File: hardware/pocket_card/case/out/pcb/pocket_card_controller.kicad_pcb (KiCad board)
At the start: 2 copper layers, 75 x 37 mm, 17 parts, among them U1 SOIC-28W_7.5x17.9mm_P1.27mm

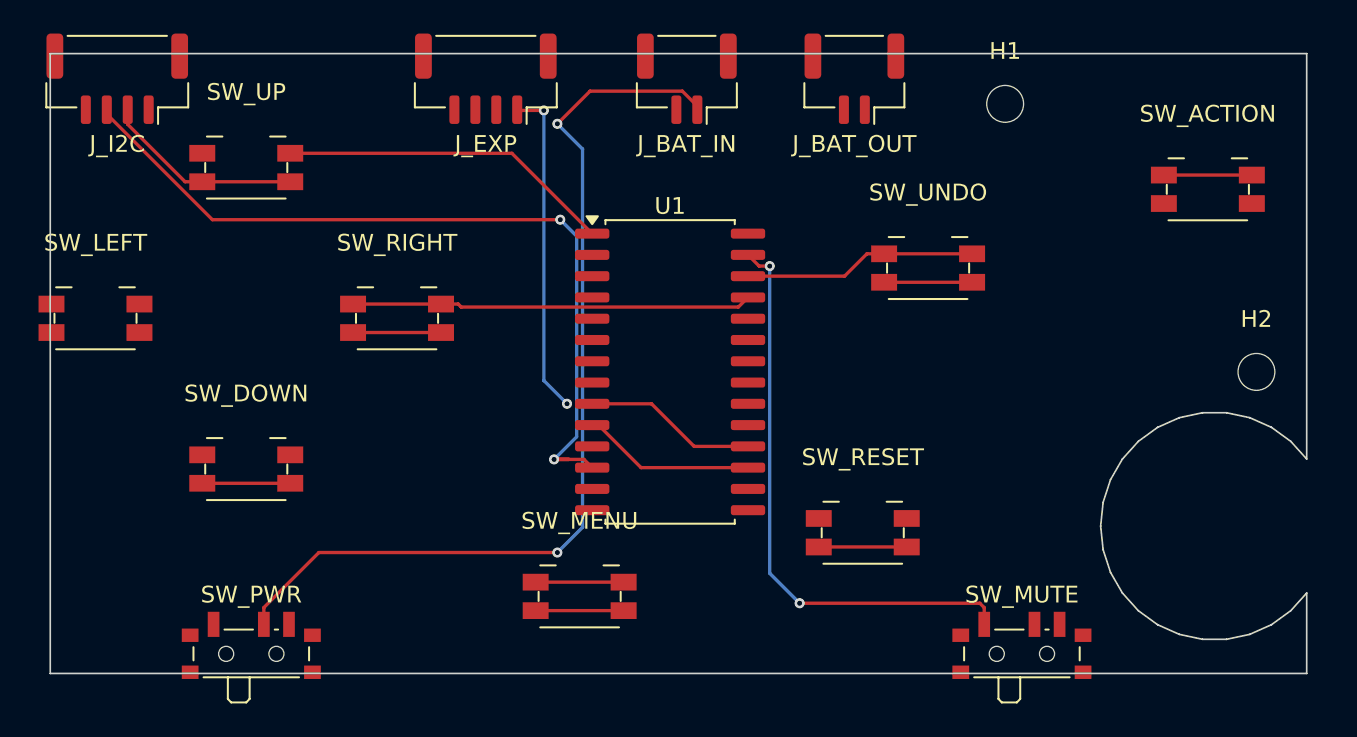
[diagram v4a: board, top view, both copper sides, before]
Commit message: Real grille: the PuzzleScript man; speaker is rectangular
The speaker is 14 x 20 x 3.5 mm, not the disc the geometry had assumed
since the design session. Driver pocket, back-shell fence and PCB notch
are all rectangular now.

That forced the grille to move. At the old (77.5, 81.2) a 14 x 20 driver
overlapped the corner boss by 0.6 mm; at (76, 80) the tightest neighbour
is the Undo collar at +0.6 mm.

The grille is the PuzzleScript man drawn as horizontal slats, generated
from a bitmap in params so the figure can be edited as text:

    01110      head
    01110
    11111      arms
    01110      body
    01010      legs

Runs of 1 are cut and the gaps between rows are the webs holding the
face together. The bottom row is two separate runs, so the five-row
figure is six slots. Square 2.6 mm pixels, 13 x 13 mm overall, sitting
inside the 14 x 20 driver footprint.

Co-Authored-By: Claude Opus 5 <noreply@anthropic.com>
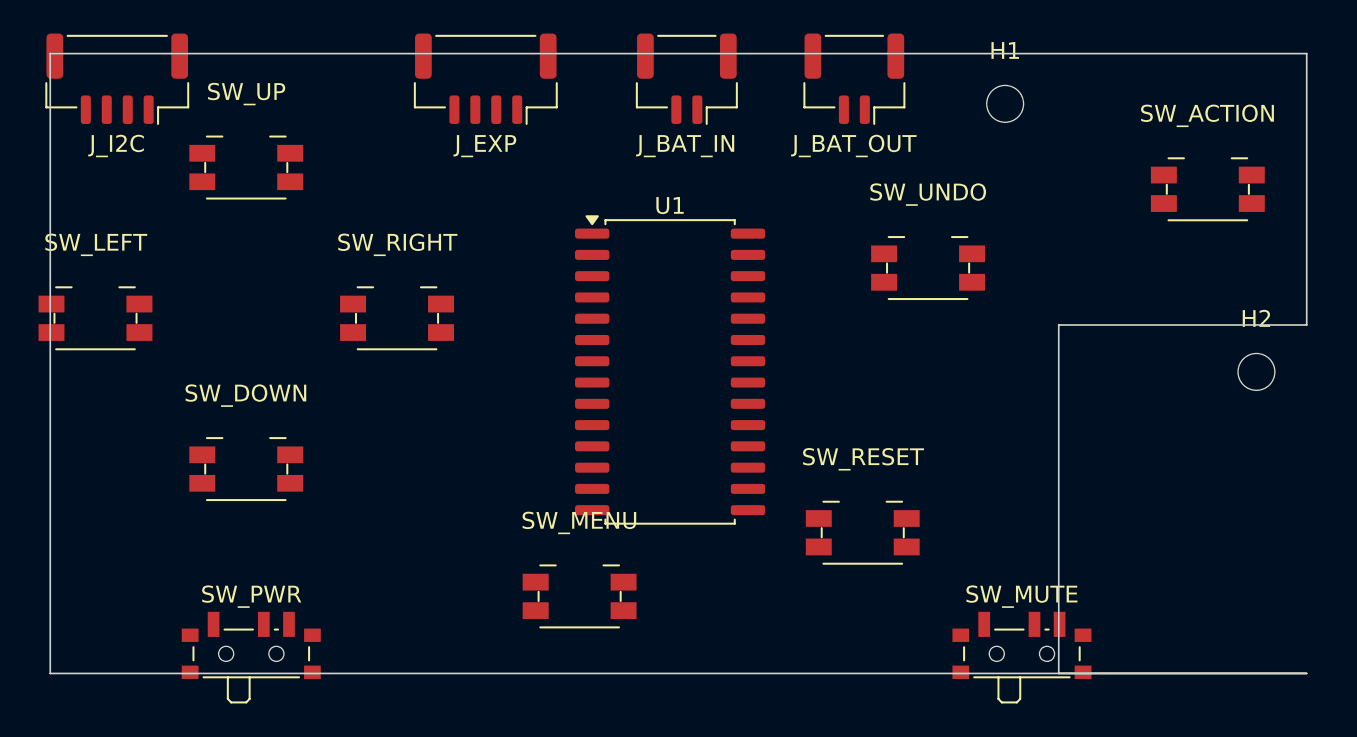
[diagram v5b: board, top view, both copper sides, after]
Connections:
- J_BAT_IN pad 1: BAT_P -> (no net)
- J_BAT_IN pad 2: GND -> (no net)
- J_BAT_OUT pad 1: BAT_SW -> (no net)
- J_BAT_OUT pad 2: GND -> (no net)
- J_EXP pad 1: INT -> (no net)
- J_I2C pad 1: +3V3 -> (no net)
- J_I2C pad 2: GND -> (no net)
- J_I2C pad 3: SCL -> (no net)
- J_I2C pad 4: SDA -> (no net)
- SW_ACTION pad 1: SIG_ACTION -> (no net)
- SW_ACTION pad 2: GND -> (no net)
- SW_DOWN pad 1: SIG_DOWN -> (no net)
- SW_DOWN pad 2: GND -> (no net)
- SW_LEFT pad 1: SIG_LEFT -> (no net)
- SW_LEFT pad 2: GND -> (no net)
- SW_MENU pad 1: SIG_MENU -> (no net)
- SW_MENU pad 2: GND -> (no net)
- SW_MUTE pad : GND -> (no net)
- SW_MUTE pad 1: SIG_MUTE -> (no net)
- SW_MUTE pad 2: GND -> (no net)
- SW_MUTE pad 3: GND -> (no net)
- SW_PWR pad 1: BAT_SW -> (no net)
- SW_PWR pad 2: BAT_P -> (no net)
- SW_RESET pad 1: SIG_RESET -> (no net)
- SW_RESET pad 2: GND -> (no net)
- SW_RIGHT pad 1: SIG_RIGHT -> (no net)
- SW_RIGHT pad 2: GND -> (no net)
- SW_UNDO pad 1: SIG_UNDO -> (no net)
- SW_UNDO pad 2: GND -> (no net)
- SW_UP pad 1: SIG_UP -> (no net)
- SW_UP pad 2: GND -> (no net)
- U1 pad 1: SIG_UP -> (no net)
- U1 pad 10: GND -> (no net)
- U1 pad 12: SCL -> (no net)
- U1 pad 13: SDA -> (no net)
- U1 pad 15: GND -> (no net)
- U1 pad 16: GND -> (no net)
- U1 pad 17: GND -> (no net)
- U1 pad 18: +3V3 -> (no net)
- U1 pad 20: INT -> (no net)
- U1 pad 21: SIG_DOWN -> (no net)
- U1 pad 22: SIG_RESET -> (no net)
- U1 pad 23: SIG_MENU -> (no net)
- U1 pad 24: SIG_LEFT -> (no net)
- U1 pad 25: SIG_RIGHT -> (no net)
- U1 pad 26: SIG_UNDO -> (no net)
- U1 pad 27: SIG_MUTE -> (no net)
- U1 pad 28: SIG_ACTION -> (no net)
- U1 pad 9: +3V3 -> (no net)
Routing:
- net BAT_P: track 56.5 -> 0.00 mm, vias 2 -> 0
- net SCL: track 51.2 -> 0.00 mm, vias 2 -> 0
- net GND: track 48.6 -> 0.00 mm
- net SIG_MUTE: track 34.6 -> 0.00 mm, vias 2 -> 0
- net SIG_RIGHT: track 23.9 -> 0.00 mm
- net SIG_UP: track 20.0 -> 0.00 mm
- net INT: track 19.7 -> 0.00 mm, vias 2 -> 0
- net SIG_UNDO: track 13.9 -> 0.00 mm
- net +3V3: track 10.4 -> 0.00 mm
- net SIG_MENU: track 5.25 -> 0.00 mm
- net SIG_ACTION: track 5.25 -> 0.00 mm
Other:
- outline, holes or cut-outs redrawn

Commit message: Run freerouting headless; fix degenerate board outline
freerouting was being launched WITHOUT --gui.enabled=false, so every
invocation opened a window and waited for a human to save. The owner was
clicking through dialogs each time without me realising. Track counts of
11, 47, 80 and 195 across runs looked like router variance; they were
just different moments at which someone pressed save. Now headless and
deterministic, with -dct 1 so dialogs cannot block.

Separately: the rectangular driver notch reached the board's bottom edge
exactly, emitting a zero-length segment that KiCad rejected as an
invalid outline. That case is a corner bite, not a pocket, and is now
handled as one.

Ground is still unrouted -- ~25 connections with no plane -- which is
what the remaining unrouted count is. The pour is the fix and needs one
manual step in the GUI, because board.Save() segfaults with a zone
present.

Co-Authored-By: Claude Opus 5 <noreply@anthropic.com>
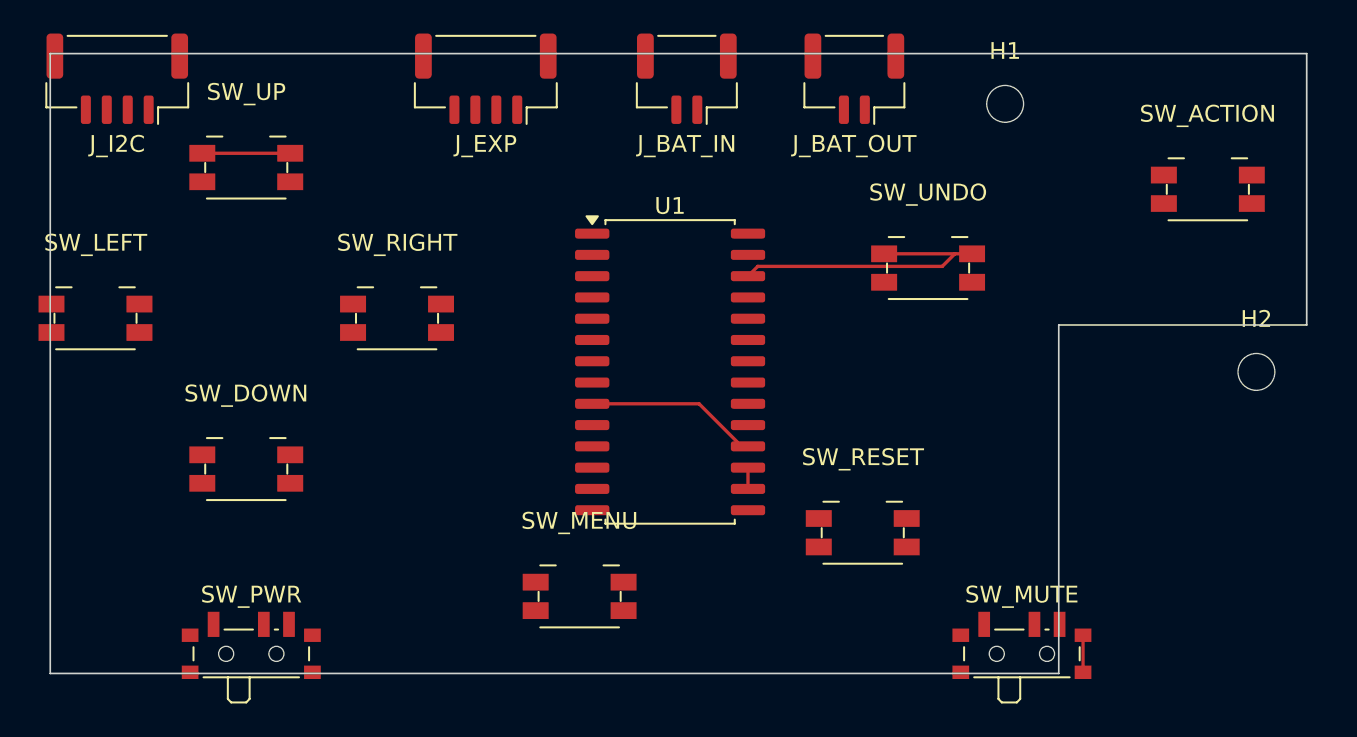
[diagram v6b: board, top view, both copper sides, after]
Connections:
- J_BAT_IN pad 1: (no net) -> BAT_P
- J_BAT_IN pad 2: (no net) -> GND
- J_BAT_OUT pad 1: (no net) -> BAT_SW
- J_BAT_OUT pad 2: (no net) -> GND
- J_EXP pad 1: (no net) -> INT
- J_I2C pad 1: (no net) -> +3V3
- J_I2C pad 2: (no net) -> GND
- J_I2C pad 3: (no net) -> SCL
- J_I2C pad 4: (no net) -> SDA
- SW_ACTION pad 1: (no net) -> SIG_ACTION
- SW_ACTION pad 2: (no net) -> GND
- SW_DOWN pad 1: (no net) -> SIG_DOWN
- SW_DOWN pad 2: (no net) -> GND
- SW_LEFT pad 1: (no net) -> SIG_LEFT
- SW_LEFT pad 2: (no net) -> GND
- SW_MENU pad 1: (no net) -> SIG_MENU
- SW_MENU pad 2: (no net) -> GND
- SW_MUTE pad : (no net) -> GND
- SW_MUTE pad 1: (no net) -> SIG_MUTE
- SW_MUTE pad 2: (no net) -> GND
- SW_MUTE pad 3: (no net) -> GND
- SW_PWR pad 1: (no net) -> BAT_SW
- SW_PWR pad 2: (no net) -> BAT_P
- SW_RESET pad 1: (no net) -> SIG_RESET
- SW_RESET pad 2: (no net) -> GND
- SW_RIGHT pad 1: (no net) -> SIG_RIGHT
- SW_RIGHT pad 2: (no net) -> GND
- SW_UNDO pad 1: (no net) -> SIG_UNDO
- SW_UNDO pad 2: (no net) -> GND
- SW_UP pad 1: (no net) -> SIG_UP
- SW_UP pad 2: (no net) -> GND
- U1 pad 1: (no net) -> SIG_UP
- U1 pad 10: (no net) -> GND
- U1 pad 12: (no net) -> SCL
- U1 pad 13: (no net) -> SDA
- U1 pad 15: (no net) -> GND
- U1 pad 16: (no net) -> GND
- U1 pad 17: (no net) -> GND
- U1 pad 18: (no net) -> +3V3
- U1 pad 20: (no net) -> INT
- U1 pad 21: (no net) -> SIG_DOWN
- U1 pad 22: (no net) -> SIG_RESET
- U1 pad 23: (no net) -> SIG_MENU
- U1 pad 24: (no net) -> SIG_LEFT
- U1 pad 25: (no net) -> SIG_RIGHT
- U1 pad 26: (no net) -> SIG_UNDO
- U1 pad 27: (no net) -> SIG_MUTE
- U1 pad 28: (no net) -> SIG_ACTION
- U1 pad 9: (no net) -> +3V3
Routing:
- net SIG_UNDO: track 0.00 -> 18.2 mm
- net +3V3: track 0.00 -> 10.4 mm
- net SIG_UP: track 0.00 -> 5.25 mm
- net GND: track 0.00 -> 3.48 mm
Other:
- outline, holes or cut-outs redrawn

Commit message: Inject the ground pour as text; manual step reduced to one keypress
pcbnew segfaults on Save() whenever a zone is present. Not the zone
settings -- an identical zone saves fine from a minimal script. Not the
destination path either. I did not find the cause.

Sidestepped: .kicad_pcb is s-expression text, and the exact syntax came
from KiCad's own writer. The two ground zones are now written into the
file directly. KiCad parses them correctly on both layers with net GND.

They are UNFILLED, so they carry no copper yet and DRC still counts
ground as unconnected. Filling is one keypress in the GUI. inject_zones
is a no-op if zones already exist, so re-running cannot duplicate them
or destroy a fill.

Also drops routing passes from 100 to 12 -- headless runs were exceeding
ten minutes and the score plateaus long before then.

Co-Authored-By: Claude Opus 5 <noreply@anthropic.com>
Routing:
- net GND: track 3.48 -> 147.8 mm
- net BAT_SW: track 0.00 -> 103.5 mm, vias 0 -> 2
- net +3V3: track 10.4 -> 44.1 mm
- net SIG_MENU: track 0.00 -> 21.6 mm
- net SIG_UNDO: track 18.2 -> 0.00 mm
- net SIG_RIGHT: track 0.00 -> 5.25 mm
- net SIG_DOWN: track 0.00 -> 5.25 mm
- added copper zone on B.Cu, net GND
- added copper zone on F.Cu, net GND

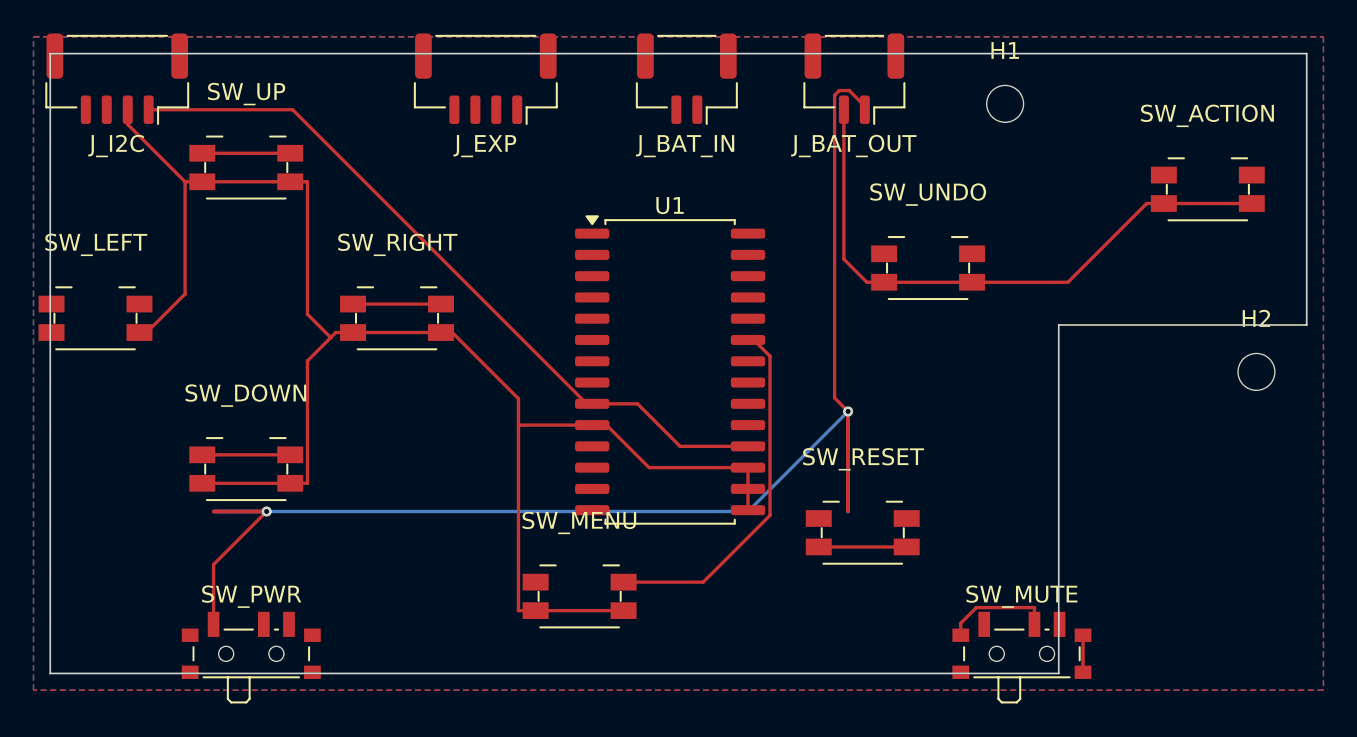
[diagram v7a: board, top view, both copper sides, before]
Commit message: Fix mounting hole floating in the driver notch; re-route succeeds
H2 sat at (80, 72), inside the bite the rectangular driver notch takes
out of the bottom-right corner -- a mounting hole in empty space where
there is no board. Introduced when the driver went from a Ø12 disc to
14 x 20 and I moved the notch without rechecking the holes. Found by the
owner looking at the board, not by any check.

Moved to (66, 81), in the narrow strip between the cell fence (x <=
60.8) and the notch (x >= 68.2). Screws must clear the cell as well as
land on board: a screw head protruding into a lithium pouch is a
puncture risk, not just untidy.

PCB_MOUNTS moves to params.py so checks.py can validate it, and
check_pcb_mounts now asserts each hole is on board material, out of the
notch, and off the cell.

Re-routing against the poured board works: 6 unrouted, down from 46.
127 tracks, 12 vias. Ground carried by the plane was the whole blocker.

Co-Authored-By: Claude Opus 5 <noreply@anthropic.com>
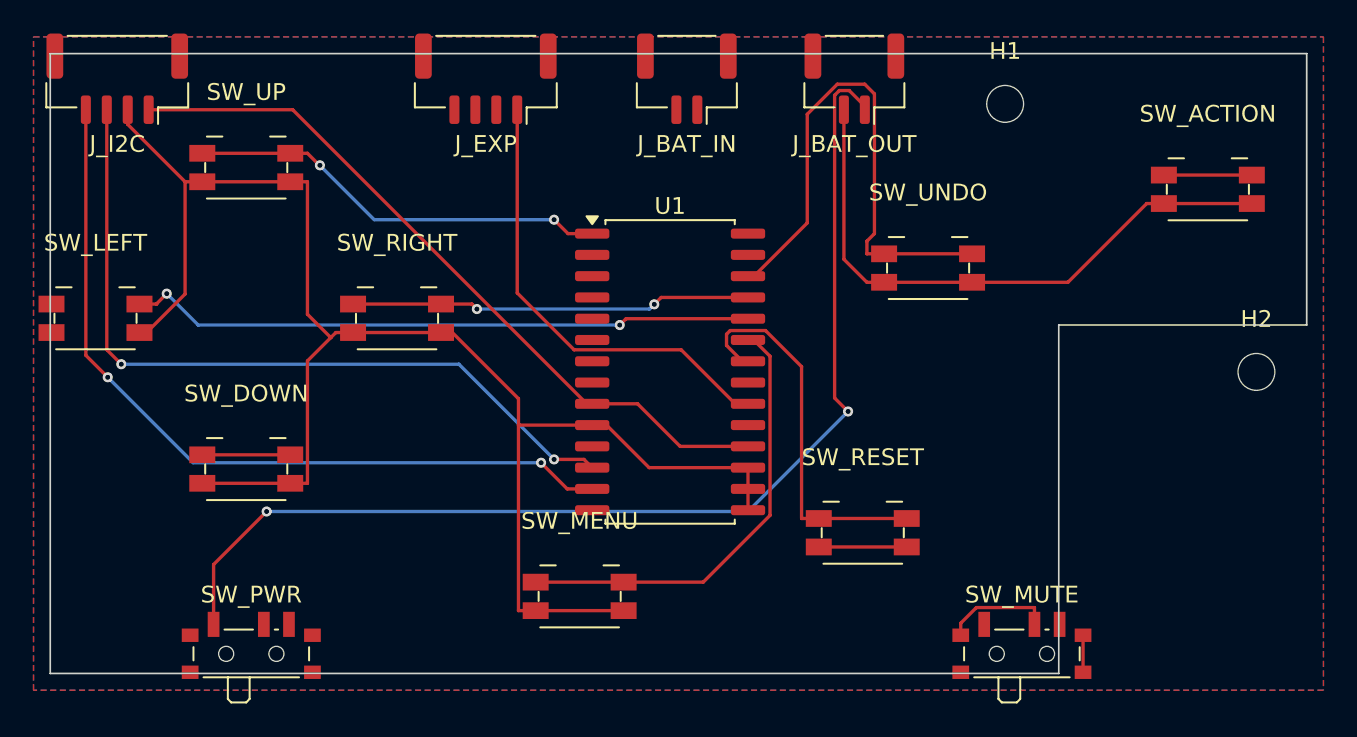
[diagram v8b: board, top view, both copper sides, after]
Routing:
- net SDA: track 0.00 -> 48.2 mm, vias 0 -> 2
- net SCL: track 0.00 -> 46.2 mm, vias 0 -> 2
- net SIG_LEFT: track 0.00 -> 37.5 mm, vias 0 -> 2
- net BAT_SW: track 103.5 -> 67.0 mm
- net SIG_UNDO: track 0.00 -> 32.3 mm
- net INT: track 0.00 -> 27.5 mm
- net SIG_RESET: track 0.00 -> 23.1 mm
- net SIG_UP: track 5.25 -> 25.3 mm, vias 0 -> 2
- net SIG_RIGHT: track 5.25 -> 24.0 mm, vias 0 -> 2
- net SIG_MENU: track 21.6 -> 26.9 mm
- net SIG_ACTION: track 0.00 -> 5.25 mm
